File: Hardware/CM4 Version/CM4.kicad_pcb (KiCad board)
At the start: 4 copper layers, 57 x 79.3 mm, 127 parts, among them IC1 TPS62111RSAT, IC2 STM32H747IIT6, J1 UART, J10 Conn_01x04, J11 Conn_01x06, J12 TSW-101-08-G-T-RA, J13 USB_B_Micro, J14 SWDIO, J15 Micro_SD_Card, J16 Conn_01x03_Female, J2 USB_C_Receptacle_USB2.0, J3 Conn_01x02, J4 32K101-400L5, J5 TSW-101-08-G-T-RA, J6 TSW-101-08-G-T-RA, J7 TSW-101-08-G-T-RA, J8 TSW-101-08-G-T-RA, J9 Conn_01x02, Q1 AO3401A, Q2 BC817W, U1 BMP280, U2 MAX-M8Q, U3 LSM9DS1, U4 USBLC6-2SC6, Y1 16MHz

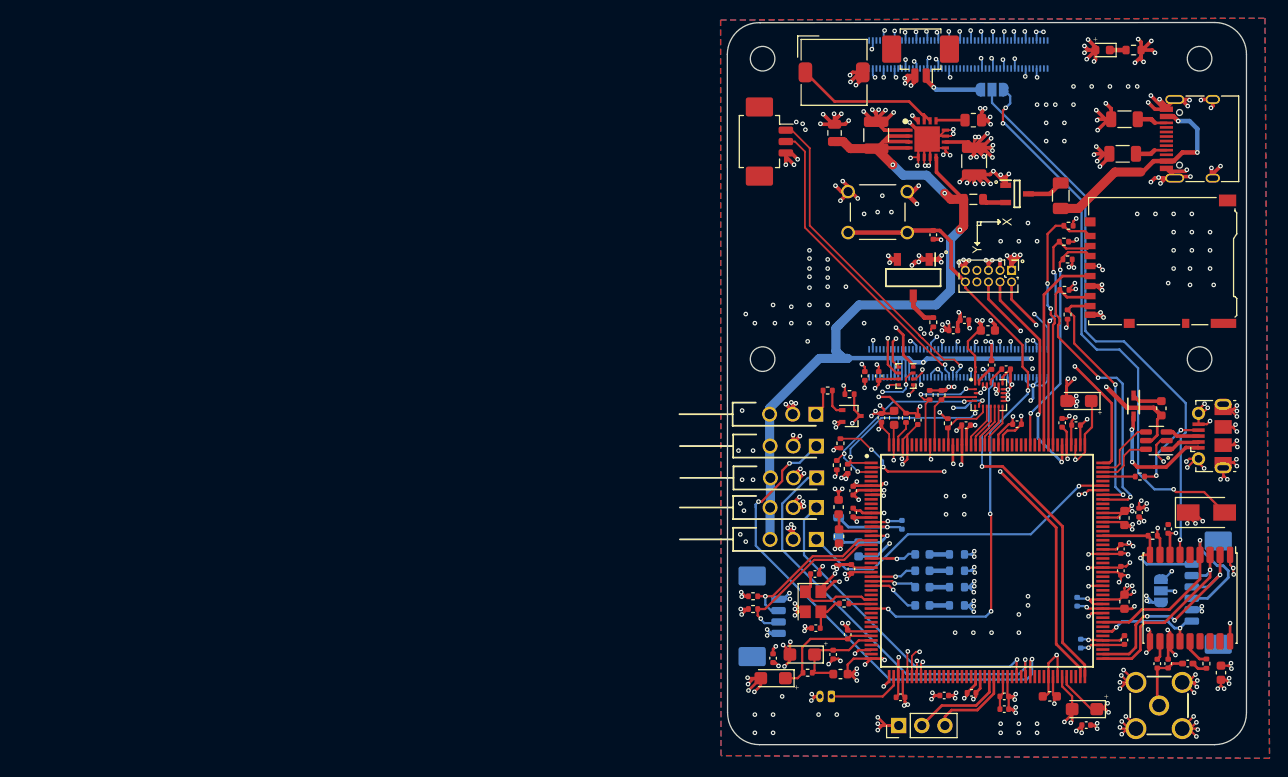
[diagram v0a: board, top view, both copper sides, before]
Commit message: Remove CM4-Backups
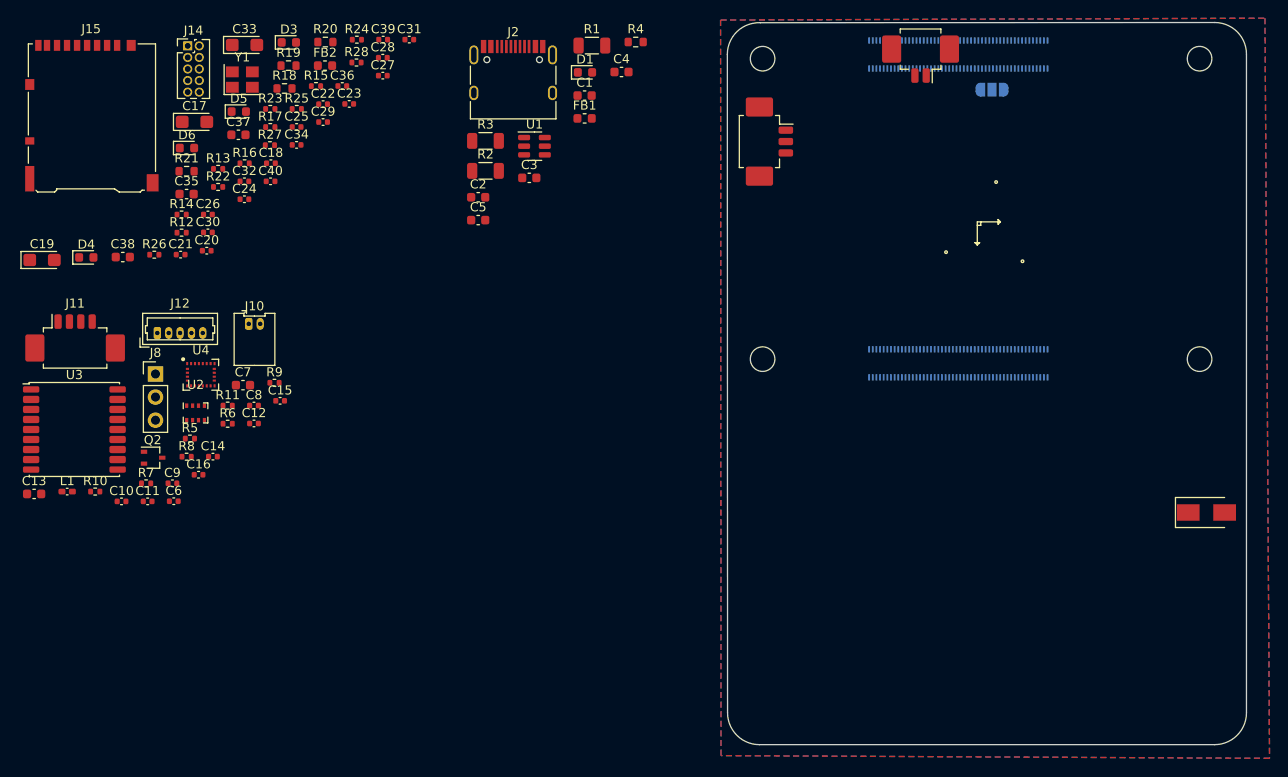
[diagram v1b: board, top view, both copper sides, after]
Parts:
- removed C41, C43: 10u, Capacitor_SMD:C_0603_1608Metric
- removed C42: 220p, Capacitor_SMD:C_0402_1005Metric
- removed C44: 1u_X5R_0603, Capacitor_SMD:C_0603_1608Metric
- removed C45, C46: 4.7u, Capacitor_SMD:C_0603_1608Metric
- removed C47: 4.7u, Capacitor_Tantalum_SMD:CP_EIA-3216-18_Kemet-A
- removed C48, C52: 100n, Capacitor_SMD:C_0402_1005Metric
- removed C49: 2.2u, Capacitor_SMD:C_0603_1608Metric
- removed C50, C51: 12p, Capacitor_SMD:C_0402_1005Metric
- removed D7: LED_Red, LED_SMD:LED_0603_1608Metric
- removed F1: Polyfuse, Fuse:Fuse_1206_3216Metric
- removed FB3, FB4: 18 @100Mhz, Inductor_SMD:L_0603_1608Metric
- removed IC1: TPS62111RSAT, SamacSys_Parts:QFN65P400X400X100-17N-D
- removed IC2: STM32H747IIT6, SamacSys_Parts:QFP50P2600X2600X160-176N
- removed J13: USB_B_Micro, Connector_USB:USB_Micro-B_Molex-105017-0001
- removed J16: Conn_01x03_Female, Connector_PinHeader_2.54mm:PinHeader_1x03_P2.54mm_Vertical
- removed J4: 32K101-400L5, SamacSys_Parts:32K101-400L5
- removed J5, J6, J7: TSW-101-08-G-T-RA, SamacSys_Parts:HDRRA3W64P254_3X1_254X254X810P
- removed J9: Conn_01x02, Connector_Molex:Molex_PicoBlade_53048-0210_1x02_P1.25mm_Horizontal
- removed JP2: SolderJumper_3_Open, Jumper:SolderJumper-3_P1.3mm_Open_RoundedPad1.0x1.5mm
- removed L2: 27n, Inductor_SMD:L_0402_1005Metric_Pad0.77x0.64mm_HandSolder
- removed L3: 2.2uH, Inductor_SMD:L_0805_2012Metric
- removed Q1: AO3401A, SamacSys_Parts:SOT95P280X125-3N
- removed R29, R30, R31: 47k, Resistor_SMD:R_0402_1005Metric
- removed R32: 10k, Resistor_SMD:R_0402_1005Metric
- removed S1: TL1105CF160Q, SamacSys_Parts:TL1105CF160Q
- removed S2: TDD01H0SB1R, SamacSys_Parts:SOT175P420X230-3N
- added R19: 2k2, Resistor_SMD:R_0603_1608Metric, F.Cu at (74.8, 47.7)
- added R20: 2k2, Resistor_SMD:R_0603_1608Metric, F.Cu at (78.8, 45.1)
- C1: value 10u x5R 25V -> 10u; footprint Capacitor_SMD:C_1210_3225Metric -> Capacitor_SMD:C_0603_1608Metric
- C10: value 10u -> 100n; footprint Capacitor_SMD:C_0603_1608Metric -> Capacitor_SMD:C_0402_1005Metric
- C11: value 100n -> 10n
- C12: value 10n -> 100n
- C13: value 10n -> 10u; footprint Capacitor_SMD:C_0402_1005Metric -> Capacitor_SMD:C_0603_1608Metric
- C15: value 4.7u -> 10n; footprint Capacitor_Tantalum_SMD:CP_EIA-3216-18_Kemet-A -> Capacitor_SMD:C_0402_1005Metric
- C17: value 100n -> 1u; footprint Capacitor_SMD:C_0402_1005Metric -> Capacitor_Tantalum_SMD:CP_EIA-3216-18_Kemet-A
- C18, D4, D5, D6: moved to F.Cu
- C19: value 100n -> 4.7u; footprint Capacitor_SMD:C_0402_1005Metric -> Capacitor_Tantalum_SMD:CP_EIA-3216-18_Kemet-A
- C2: value 22u x7R 10V -> 10u; footprint Capacitor_SMD:C_1210_3225Metric -> Capacitor_SMD:C_0603_1608Metric
- C25, C27: value 1u -> 100n; footprint Capacitor_Tantalum_SMD:CP_EIA-3216-18_Kemet-A -> Capacitor_SMD:C_0402_1005Metric
- C3: footprint Capacitor_SMD:C_0805_2012Metric -> Capacitor_SMD:C_0603_1608Metric
- C33: value 100n -> 1u; footprint Capacitor_SMD:C_0402_1005Metric -> Capacitor_Tantalum_SMD:CP_EIA-3216-18_Kemet-A; moved to F.Cu
- C35, C37: value 100n -> 2.2u; footprint Capacitor_SMD:C_0402_1005Metric -> Capacitor_SMD:C_0603_1608Metric
- C36: value 100n -> 1u
- C38: value 100n -> 1u_X5R_0603; footprint Capacitor_SMD:C_0402_1005Metric -> Capacitor_SMD:C_0603_1608Metric
- C39, C40: value 100n -> 12p
- C5: value 100n -> 1u; footprint Capacitor_SMD:C_0402_1005Metric -> Capacitor_SMD:C_0603_1608Metric
- C7: value 100n -> 10u; footprint Capacitor_SMD:C_0402_1005Metric -> Capacitor_SMD:C_0603_1608Metric
- C9: value 22p -> 100n
- D3: value SD103AWS-TP -> LED_Red; footprint SamacSys_Parts:SOD2512X115N -> LED_SMD:LED_0603_1608Metric
- FB1: value 600 @ 100MHz -> 100 @ 100MHz; footprint Inductor_SMD:L_0805_2012Metric -> Inductor_SMD:L_0603_1608Metric
- J10: value Conn_01x04 -> Conn_01x02; footprint Connector_Molex:Molex_PicoBlade_53261-0471_1x04-1MP_P1.25mm_Horizontal -> Connector_Molex:Molex_PicoBlade_53048-0210_1x02_P1.25mm_Horizontal; moved to F.Cu
- J11: value Conn_01x06 -> Conn_01x04; footprint Connector_Molex:Molex_PicoBlade_53261-0671_1x06-1MP_P1.25mm_Horizontal -> Connector_Molex:Molex_PicoBlade_53261-0471_1x04-1MP_P1.25mm_Horizontal; moved to F.Cu
- J12: value TSW-101-08-G-T-RA -> Conn_01x05; footprint SamacSys_Parts:HDRRA3W64P254_3X1_254X254X810P -> Connector_Molex:Molex_PicoBlade_53047-0510_1x05_P1.25mm_Vertical
- J8: value TSW-101-08-G-T-RA -> Conn_01x03_Female; footprint SamacSys_Parts:HDRRA3W64P254_3X1_254X254X810P -> Connector_PinHeader_2.54mm:PinHeader_1x03_P2.54mm_Vertical
- L1: value 6.8u -> 27n; footprint Inductor_SMD:L_TDK_SLF7032 -> Inductor_SMD:L_0402_1005Metric_Pad0.77x0.64mm_HandSolder
- R1: value 1M -> 5.1k; footprint Resistor_SMD:R_0805_2012Metric -> Resistor_SMD:R_1206_3216Metric
- R11: value 10k -> 1k
- R12: value 1k -> 10k
- R14: value 10k -> 4k7
- R18: value 4k7 -> 2k2; footprint Resistor_SMD:R_0402_1005Metric -> Resistor_SMD:R_0603_1608Metric
- R2: value 2.2k -> 5.1k; footprint Resistor_SMD:R_0603_1608Metric -> Resistor_SMD:R_1206_3216Metric
- R21: value 560 -> 2k2; footprint Resistor_SMD:R_0402_1005Metric -> Resistor_SMD:R_0603_1608Metric
- R22: value 2k2 -> 47; footprint Resistor_SMD:R_0603_1608Metric -> Resistor_SMD:R_0402_1005Metric; moved to F.Cu
- R23, R24, R25: value 2k2 -> 47k; footprint Resistor_SMD:R_0603_1608Metric -> Resistor_SMD:R_0402_1005Metric; moved to F.Cu
- R26: value 47 -> 47k
- R28: value 47k -> 10k
- R3: value 5.1k -> 470
- R4: value 5.1k -> 2.2k; footprint Resistor_SMD:R_1206_3216Metric -> Resistor_SMD:R_0603_1608Metric
- U1: value BMP280 -> USBLC6-2SC6; footprint Package_LGA:Bosch_LGA-8_2x2.5mm_P0.65mm_ClockwisePinNumbering -> Package_TO_SOT_SMD:SOT-23-6
- U2: value MAX-M8Q -> BMP280; footprint RF_GPS:ublox_MAX -> Package_LGA:Bosch_LGA-8_2x2.5mm_P0.65mm_ClockwisePinNumbering
- U3: value LSM9DS1 -> MAX-M8Q; footprint Package_LGA:LGA-24L_3x3.5mm_P0.43mm -> RF_GPS:ublox_MAX
- U4: value USBLC6-2SC6 -> LSM9DS1; footprint Package_TO_SOT_SMD:SOT-23-6 -> Package_LGA:LGA-24L_3x3.5mm_P0.43mm
- moved J11 128.0 mm to (51.3, 78.2), turned to 0 degrees
- moved J15 118.5 mm to (53.2, 53.2), turned to 0 degrees
- moved R5 114.4 mm to (63.9, 88.7), turned to 0 degrees
- moved C33 113.0 mm to (69.9, 45.4), turned to 0 degrees
- moved C17 112.0 mm to (64.4, 53.9), turned to 0 degrees
- moved U2 111.1 mm to (64.6, 85.9), turned to 0 degrees
- moved C9 110.0 mm to (62.0, 93.6), turned to 0 degrees
- moved R21 110.0 mm to (63.6, 59.3), turned to 0 degrees
- moved C21 109.0 mm to (62.9, 68.5), turned to 0 degrees
- moved C40 107.7 mm to (72.8, 60.4), turned to 0 degrees
- moved C13 107.6 mm to (46.8, 94.8)
- moved C35 105.4 mm to (63.6, 61.8), turned to 0 degrees
- moved U4 105.2 mm to (65.1, 81.7), turned to 0 degrees
- moved C38 104.8 mm to (56.6, 68.7), turned to 0 degrees
- moved C12 103.8 mm to (71.0, 87.0), turned to 0 degrees
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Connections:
- C1 pad 1: /5V -> VDDLDO
- C10 pad 1: /+3.3V -> VDDLDO
- C11 pad 1: /+3.3V -> Net-(C11-Pad1)
- C12 pad 1: Net-(C12-Pad1) -> VDDLDO
- C13 pad 1: Net-(C13-Pad1) -> VDDLDO
- C14 pad 1: Net-(C14-Pad1) -> VDDLDO
- C15 pad 1: /+3.3V -> Net-(C15-Pad1)
- C16 pad 1: /+3.3V -> Net-(C16-Pad1)
- C17 pad 1: /+3.3V -> /MCU/VREF+
- C18 pad 1: /+3.3V -> GND
- C18 pad 2: GND -> /MCU/VREF+
- C19 pad 1: /+3.3V -> VDDLDO
- C2 pad 1: /+3.3V -> +5V
- C20 pad 1: /+3.3V -> VDDLDO
- C21 pad 1: /+3.3V -> VDDLDO
- C22 pad 1: /+3.3V -> VDDLDO
- C23 pad 1: /+3.3V -> VDDLDO
- C24 pad 1: /+3.3V -> VDDLDO
- C25 pad 1: /MCU/VREF+ -> VDDLDO
- C26 pad 1: GND -> VDDLDO
- C26 pad 2: /MCU/VREF+ -> GND
- C27 pad 1: /MCU/+3.3VA -> VDDLDO
- C28 pad 1: GND -> VDDLDO
- C28 pad 2: /MCU/+3.3VA -> GND
- C29 pad 1: /+3.3V -> VDDLDO
- C3 pad 1: /5V -> Net-(C3-Pad1)
- C30 pad 1: /+3.3V -> VDDLDO
- C31 pad 1: /+3.3V -> VDDLDO
- C32 pad 1: /+3.3V -> VDDLDO
- C33 pad 1: /+3.3V -> /MCU/+3.3VA
- C34 pad 1: /+3.3V -> GND
- C34 pad 2: GND -> /MCU/+3.3VA
- C35 pad 1: /+3.3V -> VCAP
- C36 pad 1: /+3.3V -> /MCU/VBAT
- C37 pad 1: /+3.3V -> VCAP
- C38 pad 1: /+3.3V -> VDDLDO
- C39 pad 1: /+3.3V -> GND
- C39 pad 2: GND -> Net-(C39-Pad2)
- C4 pad 1: /+3.3V -> Net-(C4-Pad1)
- C40 pad 1: /+3.3V -> /MCU/HSE_IN
- C5 pad 1: /+3.3V -> Net-(C5-Pad1)
- C6 pad 1: /+3.3V -> VDDLDO
- C7 pad 1: /+3.3V -> VDDLDO
- C8 pad 1: /+3.3V -> VDDLDO
- C9 pad 1: Net-(C12-Pad1) -> VDDLDO
- C9 pad 2: Net-(C9-Pad2) -> GND
- D1 pad 2: /+3.3V -> VDDLDO
- D2 pad 1: /+3.3V -> VDDLDO
- D3 pad 2: Net-(D3-Pad2) -> /MCU/LED_B
- D4 pad 2: /MCU/LED_B -> /MCU/LED_D
- D5 pad 2: /MCU/LED_D -> /MCU/LED_A
- D6 pad 2: /MCU/LED_A -> /MCU/LED_C
- FB1 pad 2: /5V -> +5V
- FB2 pad 1: /+3.3V -> VDDLDO
- J10 pad 1: /+3.3V -> ANALOG_IN
- J10 pad 2: I2C2_SCL -> GND
- J11 pad 1: M8Q_NRST -> VDDLDO
- J11 pad 2: M8Q_RX -> I2C2_SCL
- J11 pad 3: M8Q_TX -> I2C2_SDA
- J11 pad 4: M8Q_PPS -> GND
- J12 pad 1: SBUS_IN -> M8Q_NRST
- J12 pad 2: GND -> M8Q_RX
- J12 pad 3: /5V -> M8Q_TX
- J14 pad 1: /+3.3V -> VDDLDO
- J14 pad 7: no_connect_163 -> unconnected-(J14-Pad7)
- J14 pad 8: no_connect_164 -> unconnected-(J14-Pad8)
- J15 pad 4: /+3.3V -> VDDLDO
- J2 pad A6: no_connect_165 -> /Power/USB_D+
- J2 pad A7: no_connect_166 -> /Power/USB_D-
- J2 pad A8: no_connect_167 -> unconnected-(J2-PadA8)
- J2 pad B6: no_connect_168 -> /Power/USB_D+
- J2 pad B7: no_connect_169 -> /Power/USB_D-
- J2 pad B8: no_connect_170 -> unconnected-(J2-PadB8)
- J8 pad 1: TIM1_CH4 -> GND
- J8 pad 2: GND -> UART7_RX
- J8 pad 3: /5V -> UART7_TX
- L1 pad 1: /Power/SW -> Net-(C11-Pad1)
- L1 pad 2: /+3.3V -> Net-(J4-Pad1)
- Module1 pad 10: no_connect_171 -> unconnected-(Module1-Pad10)
- Module1 pad 100: no_connect_172 -> unconnected-(Module1-Pad100)
- Module1 pad 101: no_connect_173 -> unconnected-(Module1-Pad101)
- Module1 pad 102: no_connect_174 -> unconnected-(Module1-Pad102)
- Module1 pad 103: no_connect_175 -> unconnected-(Module1-Pad103)
- Module1 pad 104: no_connect_176 -> unconnected-(Module1-Pad104)
- Module1 pad 105: no_connect_177 -> unconnected-(Module1-Pad105)
- Module1 pad 106: no_connect_178 -> unconnected-(Module1-Pad106)
- Module1 pad 109: no_connect_179 -> unconnected-(Module1-Pad109)
- Module1 pad 11: no_connect_180 -> unconnected-(Module1-Pad11)
- Module1 pad 110: no_connect_181 -> unconnected-(Module1-Pad110)
- Module1 pad 111: no_connect_182 -> unconnected-(Module1-Pad111)
- Module1 pad 112: no_connect_183 -> unconnected-(Module1-Pad112)
- Module1 pad 115: no_connect_184 -> unconnected-(Module1-Pad115)
- Module1 pad 116: no_connect_185 -> unconnected-(Module1-Pad116)
- Module1 pad 117: no_connect_186 -> unconnected-(Module1-Pad117)
- Module1 pad 118: no_connect_187 -> unconnected-(Module1-Pad118)
- Module1 pad 12: no_connect_188 -> unconnected-(Module1-Pad12)
- Module1 pad 121: no_connect_189 -> unconnected-(Module1-Pad121)
- Module1 pad 122: no_connect_190 -> unconnected-(Module1-Pad122)
- Module1 pad 123: no_connect_191 -> unconnected-(Module1-Pad123)
- Module1 pad 124: no_connect_192 -> unconnected-(Module1-Pad124)
- Module1 pad 127: no_connect_193 -> unconnected-(Module1-Pad127)
- Module1 pad 128: no_connect_194 -> unconnected-(Module1-Pad128)
- Module1 pad 129: no_connect_195 -> unconnected-(Module1-Pad129)
- Module1 pad 130: no_connect_196 -> unconnected-(Module1-Pad130)
- Module1 pad 133: no_connect_197 -> unconnected-(Module1-Pad133)
- Module1 pad 134: no_connect_198 -> unconnected-(Module1-Pad134)
- Module1 pad 135: no_connect_199 -> unconnected-(Module1-Pad135)
- Module1 pad 136: no_connect_200 -> unconnected-(Module1-Pad136)
- Module1 pad 139: no_connect_201 -> unconnected-(Module1-Pad139)
- Module1 pad 140: no_connect_202 -> unconnected-(Module1-Pad140)
- Module1 pad 141: no_connect_203 -> unconnected-(Module1-Pad141)
- Module1 pad 142: no_connect_204 -> unconnected-(Module1-Pad142)
- Module1 pad 143: no_connect_205 -> unconnected-(Module1-Pad143)
- Module1 pad 145: no_connect_206 -> unconnected-(Module1-Pad145)
- Module1 pad 146: no_connect_207 -> unconnected-(Module1-Pad146)
- Module1 pad 147: no_connect_208 -> unconnected-(Module1-Pad147)
- Module1 pad 148: no_connect_209 -> unconnected-(Module1-Pad148)
- Module1 pad 149: no_connect_210 -> unconnected-(Module1-Pad149)
- Module1 pad 15: no_connect_211 -> unconnected-(Module1-Pad15)
- Module1 pad 151: no_connect_212 -> unconnected-(Module1-Pad151)
- Module1 pad 152: no_connect_213 -> unconnected-(Module1-Pad152)
- Module1 pad 153: no_connect_214 -> unconnected-(Module1-Pad153)
- Module1 pad 154: no_connect_215 -> unconnected-(Module1-Pad154)
- Module1 pad 157: no_connect_216 -> unconnected-(Module1-Pad157)
- Module1 pad 158: no_connect_217 -> unconnected-(Module1-Pad158)
- Module1 pad 159: no_connect_218 -> unconnected-(Module1-Pad159)
- Module1 pad 16: no_connect_219 -> unconnected-(Module1-Pad16)
- Module1 pad 160: no_connect_220 -> unconnected-(Module1-Pad160)
- Module1 pad 163: no_connect_221 -> unconnected-(Module1-Pad163)
- Module1 pad 164: no_connect_222 -> unconnected-(Module1-Pad164)
- Module1 pad 165: no_connect_223 -> unconnected-(Module1-Pad165)
- Module1 pad 166: no_connect_224 -> unconnected-(Module1-Pad166)
- Module1 pad 169: no_connect_225 -> unconnected-(Module1-Pad169)
- Module1 pad 17: no_connect_226 -> unconnected-(Module1-Pad17)
- Module1 pad 170: no_connect_227 -> unconnected-(Module1-Pad170)
- Module1 pad 171: no_connect_228 -> unconnected-(Module1-Pad171)
- Module1 pad 172: no_connect_229 -> unconnected-(Module1-Pad172)
- Module1 pad 175: no_connect_230 -> unconnected-(Module1-Pad175)
- Module1 pad 176: no_connect_231 -> unconnected-(Module1-Pad176)
- Module1 pad 177: no_connect_232 -> unconnected-(Module1-Pad177)
- Module1 pad 178: no_connect_233 -> unconnected-(Module1-Pad178)
- Module1 pad 18: no_connect_234 -> unconnected-(Module1-Pad18)
- Module1 pad 181: no_connect_235 -> unconnected-(Module1-Pad181)
- Module1 pad 182: no_connect_236 -> unconnected-(Module1-Pad182)
- Module1 pad 183: no_connect_237 -> unconnected-(Module1-Pad183)
- Module1 pad 184: no_connect_238 -> unconnected-(Module1-Pad184)
- Module1 pad 187: no_connect_239 -> unconnected-(Module1-Pad187)
- Module1 pad 188: no_connect_240 -> unconnected-(Module1-Pad188)
- Module1 pad 189: no_connect_241 -> unconnected-(Module1-Pad189)
- Module1 pad 19: no_connect_242 -> unconnected-(Module1-Pad19)
- Module1 pad 190: no_connect_243 -> unconnected-(Module1-Pad190)
- Module1 pad 193: no_connect_244 -> unconnected-(Module1-Pad193)
- Module1 pad 194: no_connect_245 -> unconnected-(Module1-Pad194)
- Module1 pad 195: no_connect_246 -> unconnected-(Module1-Pad195)
- Module1 pad 196: no_connect_247 -> unconnected-(Module1-Pad196)
- Module1 pad 199: no_connect_248 -> unconnected-(Module1-Pad199)
- Module1 pad 20: no_connect_249 -> unconnected-(Module1-Pad20)
- Module1 pad 200: no_connect_250 -> unconnected-(Module1-Pad200)
- Module1 pad 21: no_connect_251 -> unconnected-(Module1-Pad21)
- Module1 pad 24: no_connect_252 -> unconnected-(Module1-Pad24)
- Module1 pad 25: no_connect_253 -> unconnected-(Module1-Pad25)
- Module1 pad 26: no_connect_254 -> unconnected-(Module1-Pad26)
- Module1 pad 27: no_connect_255 -> unconnected-(Module1-Pad27)
- Module1 pad 29: no_connect_256 -> unconnected-(Module1-Pad29)
- Module1 pad 3: no_connect_257 -> unconnected-(Module1-Pad3)
- Module1 pad 30: no_connect_258 -> unconnected-(Module1-Pad30)
- Module1 pad 34: no_connect_259 -> unconnected-(Module1-Pad34)
- Module1 pad 35: no_connect_260 -> unconnected-(Module1-Pad35)
- Module1 pad 36: no_connect_261 -> unconnected-(Module1-Pad36)
- Module1 pad 37: no_connect_262 -> unconnected-(Module1-Pad37)
- Module1 pad 38: no_connect_263 -> unconnected-(Module1-Pad38)
- Module1 pad 39: no_connect_264 -> unconnected-(Module1-Pad39)
- Module1 pad 4: no_connect_265 -> unconnected-(Module1-Pad4)
- Module1 pad 40: no_connect_266 -> unconnected-(Module1-Pad40)
- Module1 pad 41: no_connect_267 -> unconnected-(Module1-Pad41)
- Module1 pad 44: no_connect_268 -> unconnected-(Module1-Pad44)
- Module1 pad 45: no_connect_269 -> unconnected-(Module1-Pad45)
- Module1 pad 46: no_connect_270 -> unconnected-(Module1-Pad46)
- Module1 pad 47: no_connect_271 -> unconnected-(Module1-Pad47)
- Module1 pad 48: no_connect_272 -> unconnected-(Module1-Pad48)
- Module1 pad 49: no_connect_273 -> unconnected-(Module1-Pad49)
- Module1 pad 5: no_connect_274 -> unconnected-(Module1-Pad5)
- Module1 pad 50: no_connect_275 -> unconnected-(Module1-Pad50)
- Module1 pad 54: no_connect_276 -> unconnected-(Module1-Pad54)
- Module1 pad 56: no_connect_277 -> unconnected-(Module1-Pad56)
- Module1 pad 57: no_connect_278 -> unconnected-(Module1-Pad57)
- Module1 pad 58: no_connect_279 -> unconnected-(Module1-Pad58)
- Module1 pad 6: no_connect_280 -> unconnected-(Module1-Pad6)
- Module1 pad 61: no_connect_281 -> unconnected-(Module1-Pad61)
- Module1 pad 62: no_connect_282 -> unconnected-(Module1-Pad62)
- Module1 pad 63: no_connect_283 -> unconnected-(Module1-Pad63)
- Module1 pad 64: no_connect_284 -> unconnected-(Module1-Pad64)
- Module1 pad 67: no_connect_285 -> unconnected-(Module1-Pad67)
- Module1 pad 68: no_connect_286 -> unconnected-(Module1-Pad68)
- Module1 pad 69: no_connect_287 -> unconnected-(Module1-Pad69)
- Module1 pad 70: no_connect_288 -> unconnected-(Module1-Pad70)
- Module1 pad 72: no_connect_289 -> unconnected-(Module1-Pad72)
- Module1 pad 73: no_connect_290 -> unconnected-(Module1-Pad73)
- Module1 pad 75: no_connect_291 -> unconnected-(Module1-Pad75)
- Module1 pad 76: no_connect_292 -> unconnected-(Module1-Pad76)
- Module1 pad 77: /5V -> +5V
- Module1 pad 78: no_connect_293 -> unconnected-(Module1-Pad78)
- Module1 pad 79: /5V -> +5V
- Module1 pad 80: no_connect_294 -> unconnected-(Module1-Pad80)
- Module1 pad 81: /5V -> +5V
- Module1 pad 82: no_connect_295 -> unconnected-(Module1-Pad82)
- Module1 pad 83: /5V -> +5V
- Module1 pad 84: no_connect_296 -> unconnected-(Module1-Pad84)
- Module1 pad 85: /5V -> +5V
- Module1 pad 86: no_connect_297 -> unconnected-(Module1-Pad86)
- Module1 pad 87: /5V -> +5V
- Module1 pad 88: no_connect_298 -> unconnected-(Module1-Pad88)
- Module1 pad 89: no_connect_299 -> unconnected-(Module1-Pad89)
- Module1 pad 9: no_connect_300 -> unconnected-(Module1-Pad9)
- Module1 pad 90: no_connect_301 -> unconnected-(Module1-Pad90)
- Module1 pad 91: no_connect_302 -> unconnected-(Module1-Pad91)
- Module1 pad 92: no_connect_303 -> unconnected-(Module1-Pad92)
- Module1 pad 93: no_connect_304 -> unconnected-(Module1-Pad93)
- Module1 pad 94: no_connect_305 -> unconnected-(Module1-Pad94)
- Module1 pad 95: no_connect_306 -> unconnected-(Module1-Pad95)
- Module1 pad 96: no_connect_307 -> unconnected-(Module1-Pad96)
- Module1 pad 97: no_connect_308 -> unconnected-(Module1-Pad97)
- Module1 pad 99: no_connect_309 -> unconnected-(Module1-Pad99)
- R1 pad 1: /Power/PG -> Net-(J2-PadA5)
- R1 pad 2: /+3.3V -> GND
- R10 pad 1: /+3.3V -> SBUS_RX
- R10 pad 2: LSM9DS1_CS_M -> VDDLDO
- R11 pad 1: SBUS_RX -> SBUS_IN
- R11 pad 2: /+3.3V -> Net-(Q2-Pad1)
- R12 pad 1: SBUS_IN -> VDDLDO
- R12 pad 2: Net-(Q2-Pad1) -> Net-(IC2-Pad142)
- R14 pad 1: /+3.3V -> VDDLDO
- R14 pad 2: Net-(IC2-Pad174) -> I2C1_SCL
- R15 pad 1: /+3.3V -> I2C1_SDA
- R15 pad 2: I2C1_SCL -> VDDLDO
- R16 pad 1: I2C1_SDA -> VDDLDO
- R16 pad 2: /+3.3V -> I2C2_SDA
- R17 pad 1: /+3.3V -> I2C2_SCL
- R17 pad 2: I2C2_SDA -> VDDLDO
- R18 pad 1: I2C2_SCL -> Net-(D3-Pad1)
- R18 pad 2: /+3.3V -> GND
- R2 pad 1: GND -> Net-(J2-PadB5)
- R2 pad 2: Net-(D1-Pad1) -> GND
- R21 pad 1: Net-(J13-Pad4) -> Net-(D6-Pad1)
- R21 pad 2: /MCU/USB_OTG_ID -> GND
- R22 pad 1: Net-(D4-Pad1) -> /MCU/HSE_OUT
- R22 pad 2: GND -> Net-(C39-Pad2)
- R23 pad 1: Net-(D5-Pad1) -> /MCU/SDMMC_D2
- R23 pad 2: GND -> VDDLDO
- R24 pad 1: Net-(D6-Pad1) -> /MCU/SDMMC_D3
- R24 pad 2: GND -> VDDLDO
- R25 pad 1: Net-(D7-Pad1) -> /MCU/SDMMC_CMD
- R25 pad 2: GND -> VDDLDO
- R26 pad 1: /MCU/HSE_OUT -> /MCU/SDMMC_D0
- R26 pad 2: Net-(C50-Pad2) -> VDDLDO
- R27 pad 1: /MCU/SDMMC_D2 -> /MCU/SDMMC_D1
- R27 pad 2: /+3.3V -> VDDLDO
- R28 pad 1: /MCU/SDMMC_D3 -> Net-(R28-Pad1)
- R28 pad 2: /+3.3V -> /MCU/BOOT0
- R3 pad 1: Net-(J2-PadA5) -> GND
- R3 pad 2: GND -> Net-(Q1-Pad1)
- R4 pad 1: Net-(J2-PadB5) -> GND
- R4 pad 2: GND -> Net-(D1-Pad1)
- R5 pad 2: Net-(L2-Pad1) -> Net-(C11-Pad1)
- R6 pad 1: /+3.3V -> VDDLDO
- R6 pad 2: M8Q_NRST -> LSM9DS1_SDO_M
- R7 pad 1: /+3.3V -> VDDLDO
- R7 pad 2: LSM9DS1_SDO_M -> LSM9DS1_SDO_AG
- R8 pad 1: /+3.3V -> VDDLDO
- R8 pad 2: LSM9DS1_SDO_AG -> LSM9DS1_CS_AG
- R9 pad 1: /+3.3V -> VDDLDO
- R9 pad 2: LSM9DS1_CS_AG -> LSM9DS1_CS_M
- U1 pad 1: GND -> /Power/USB_D_P
- U1 pad 2: SPI1_NCS -> GND
- U1 pad 3: SPI1_MOSI -> /Power/USB_D_N
- U1 pad 4: SPI1_SCK -> /Power/USB_D-
- U1 pad 5: SPI1_MISO -> +5V
- U1 pad 6: /+3.3V -> /Power/USB_D+
- U2 pad 2: M8Q_TX -> SPI1_NCS
- U2 pad 3: M8Q_RX -> SPI1_MOSI
- U2 pad 4: M8Q_PPS -> SPI1_SCK
- U2 pad 5: no_connect_312 -> SPI1_MISO
- U2 pad 6: M8Q_BATT -> VDDLDO
- U2 pad 7: /+3.3V -> GND
- U2 pad 8: /+3.3V -> VDDLDO
- U3 pad 1: /+3.3V -> GND
- U3 pad 10: LSM9DS1_INT_M -> GND
- U3 pad 11: LSM9DS1_INT1_AG -> Net-(J4-Pad1)
- U3 pad 12: LSM9DS1_INT2_AG -> GND
- U3 pad 13: LSM9DS1_DEN_AG -> unconnected-(U3-Pad13)
- U3 pad 14: GND -> Net-(R5-Pad1)
- U3 pad 15: GND -> unconnected-(U3-Pad15)
- U3 pad 16: GND -> unconnected-(U3-Pad16)
- U3 pad 17: GND -> unconnected-(U3-Pad17)
- U3 pad 18: GND -> unconnected-(U3-Pad18)
- U3 pad 2: I2C1_SCL -> M8Q_TX
- U3 pad 3: /+3.3V -> M8Q_RX
- U3 pad 4: I2C1_SDA -> M8Q_PPS
- U3 pad 5: LSM9DS1_SDO_AG -> unconnected-(U3-Pad5)
- U3 pad 6: LSM9DS1_SDO_M -> VDDLDO
- U3 pad 7: LSM9DS1_CS_AG -> VDDLDO
- U3 pad 8: LSM9DS1_CS_M -> VDDLDO
- U3 pad 9: LSM9DS1_DRDY_M -> M8Q_NRST
- U4 pad 1: /MCU/USB_CONN_D- -> VDDLDO
- U4 pad 2: GND -> I2C1_SCL
- U4 pad 3: /MCU/USB_CONN_D+ -> VDDLDO
- U4 pad 4: /MCU/USB_D_P -> I2C1_SDA
- U4 pad 5: /5V -> LSM9DS1_SDO_AG
- U4 pad 6: /MCU/USB_D_N -> LSM9DS1_SDO_M
- Y1 pad 3: Net-(C50-Pad2) -> Net-(C39-Pad2)
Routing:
- net GND: track 458.2 -> 0.00 mm, vias 388 -> 0
- net /+3.3V: track 201.1 -> 0.00 mm, vias 121 -> 0
- net /5V: track 142.0 -> 0.00 mm, vias 6 -> 0
- net /MCU/VCAP1: track 77.8 -> 0.00 mm, vias 4 -> 0
- net /MCU/NRST: track 71.1 -> 0.00 mm, vias 4 -> 0
- net M8Q_BATT: track 62.0 -> 0.00 mm, vias 1 -> 0
- net Net-(D2-Pad2): track 61.8 -> 0.00 mm, vias 3 -> 0
- net TIM1_CH4: track 55.2 -> 0.00 mm, vias 3 -> 0
- net TIM1_CH3: track 45.5 -> 0.00 mm, vias 1 -> 0
- net PI_GPIO13_RX_5: track 42.0 -> 0.00 mm, vias 2 -> 0
- net PI_GPIO12_TX_5: track 39.4 -> 0.00 mm, vias 1 -> 0
- net SPI1_NCS: track 37.4 -> 0.00 mm, vias 3 -> 0
- net TIM1_CH1: track 36.6 -> 0.00 mm, vias 1 -> 0
- net TIM1_CH2: track 36.5 -> 0.00 mm, vias 1 -> 0
- net SPI1_MOSI: track 36.0 -> 0.00 mm, vias 2 -> 0
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- added copper zone on In2.Cu, net VDDLDO
- removed copper zone on In2.Cu, net /+3.3V
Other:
- board text removed: "+"
- board text removed: "3.3V"
- board text removed: "ADC"
- board text removed: "CM4 FCS | Rev1"
- board text removed: "GND"
- board text removed: "I2C"
- board text removed: "LNA"
- board text removed: "PI UART"
- board text removed: "PPS"
- board text removed: "RST"
- board text removed: "RX"
- board text removed: "SCL"
- board text removed: "SDA"
- board text removed: "TX"
- board text removed: "V+"
- board text removed: "Wireless Keepout"
- board text removed: "X"
- board text removed: "Y"
